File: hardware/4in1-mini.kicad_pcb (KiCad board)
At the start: 6 copper layers, 31.2 x 33 mm, 186 parts, among them J1 SM08B-SRSS-TB, Q1 DOY180N03T, Q10 DOY180N03T, Q11 DOY180N03T, Q12 DOY180N03T, Q13 DOY180N03T, Q14 DOY180N03T, Q15 DOY180N03T, Q16 DOY180N03T, Q17 DOY180N03T, Q18 DOY180N03T, Q19 DOY180N03T, Q2 DOY180N03T, Q20 DOY180N03T, Q21 DOY180N03T, Q22 DOY180N03T, Q23 DOY180N03T, Q24 DOY180N03T, Q3 DOY180N03T, Q4 DOY180N03T, Q5 DOY180N03T, Q6 DOY180N03T, Q7 DOY180N03T, Q8 DOY180N03T, Q9 DOY180N03T, U1 TLV76733DRVR, U10 AT32F421G8U7, U11 NSG2065Q, U12 INA186A3IDCKR, U13 LMR54406DBVR, U2 AT32F421G8U7, U3 NSG2065Q, U5 FTC160808S4R7MBCA, U6 AT32F421G8U7, U7 NSG2065Q, U8 AT32F421G8U7, U9 NSG2065Q

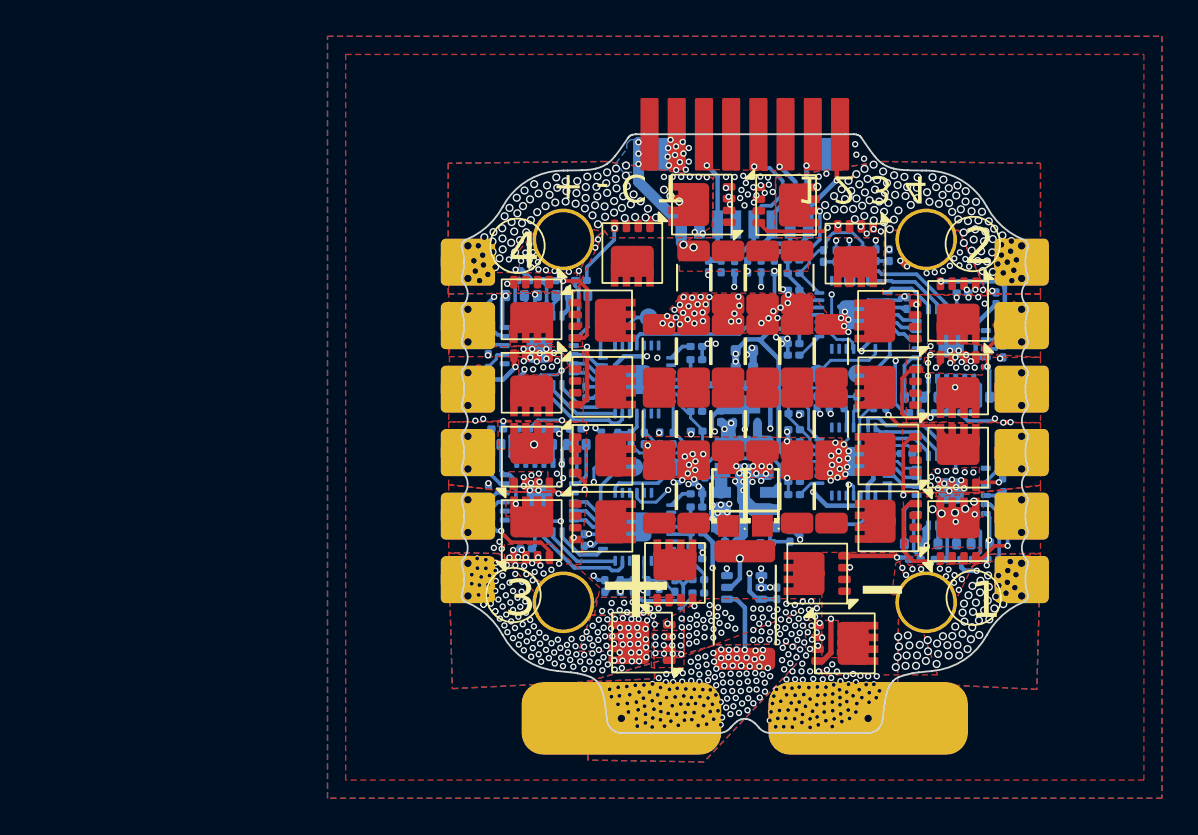
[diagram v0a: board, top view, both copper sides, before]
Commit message: Rev 3: input TVS removed
The 2x SMF24A-T13 are removed. Their 24 V standoff sits below the 25.2 V a full
6S pack reaches, so they conducted rather than protected. The board stays 6S
only and now has no input clamp; DESIGN.md updated to say so.

ERC and DRC reviewed by the maintainer.

Co-Authored-By: Claude Opus 5 (1M context) <noreply@anthropic.com>
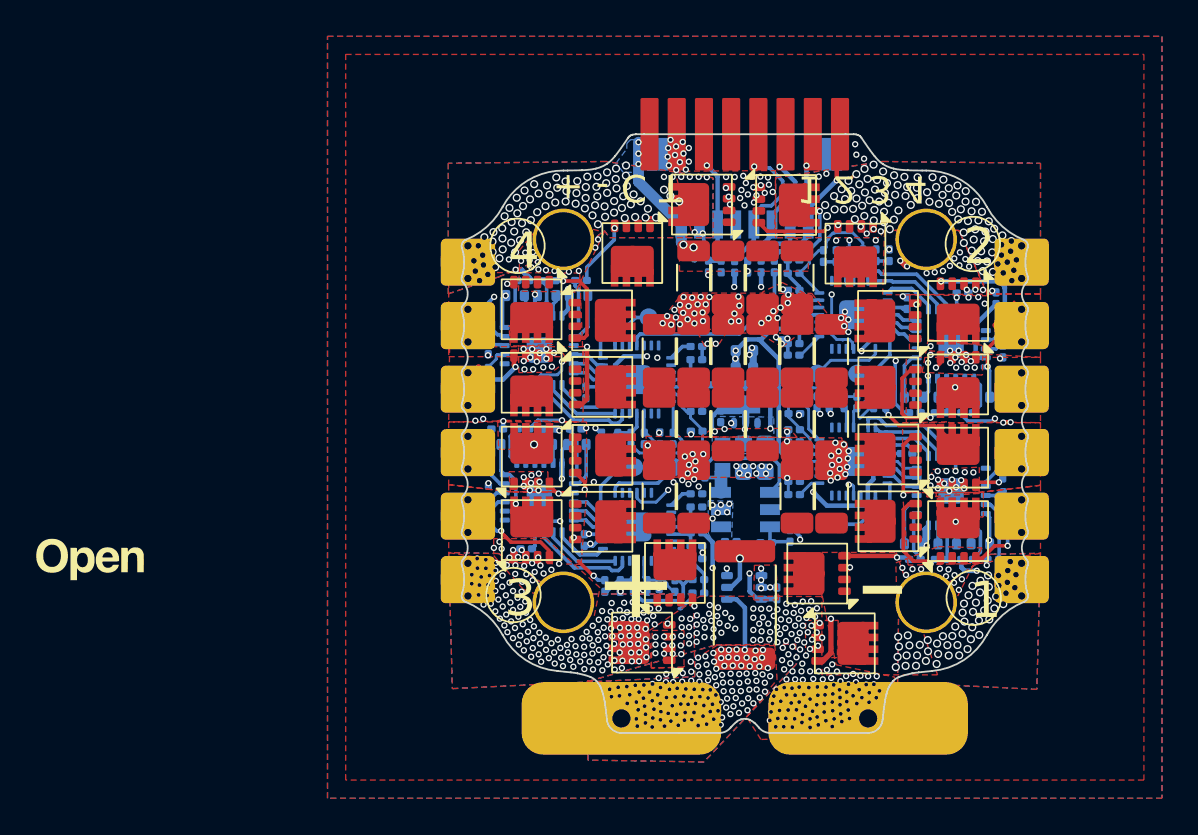
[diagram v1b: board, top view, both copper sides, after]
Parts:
- removed D1, D2: SMF24A-T13, 4in1ESC:SOD-123FL_L2.7-W1.8-LS3.7-RD
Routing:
- net GND: track 75.7 -> 28.5 mm, vias 457 -> 447
- net +10V: track 85.6 -> 78.6 mm
- net /ESC1/MotorB: track 18.8 -> 13.4 mm, vias 8 -> 2
- net +BATT: track 11.6 -> 9.99 mm
- net /ESC3/MotorC: track 13.8 -> 14.9 mm
- net /ESC4/MotorB: track 15.5 -> 14.8 mm
- net /ESC4/MotorA: track 20.1 -> 19.5 mm
- net Net-(Q20-G): track 17.5 -> 16.9 mm
- net /ESC3/MotorA: track 10.7 -> 10.6 mm, vias 144 -> 142
- net Net-(U10-PB4): vias 1 -> 0
- net /ESC2/MotorA: vias 100 -> 99
- net /CSA+: vias 140 -> 137
- added copper zone on B.Cu, net +10V
- added copper zone on In1.Cu, net /ESC1/MotorA
- added copper zone on In4.Cu, net /ESC1/MotorA
- added copper zone on In1.Cu, net /ESC2/MotorA
- added copper zone on In4.Cu, net /ESC2/MotorA
- added copper zone on In1.Cu, net /ESC3/MotorA
- added copper zone on In4.Cu, net /ESC3/MotorA
- added copper zone on In1.Cu, net /ESC4/MotorA
- added copper zone on In4.Cu, net /ESC4/MotorA
- removed copper zone on In2.Cu, net +3V3
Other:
- board text added: "2-6S"
- board text added: "rev3"
- board text removed: "3-6S"

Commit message: Rev 3.1 working state: flashing fixture, QC updates, board work
New 20x20-ESC-Flashing pogo-pin fixture project, MotorTest project file,
QC fixture and main board PCB updates, shop badge on the new gold.
Internal notes and regenerable fixture STEPs stay local via the
repo-specific .gitignore tail.

Co-Authored-By: Claude Opus 5 (1M context) <noreply@anthropic.com>
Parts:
- added CL50: 10uF, Capacitor_SMD:C_1206_3216Metric, F.Cu at (75.1, 52.4)
- added CL51: 10uF, Capacitor_SMD:C_1206_3216Metric, F.Cu at (77.0, 52.4)
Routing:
- net /ESC4/MotorA: vias 85 -> 82

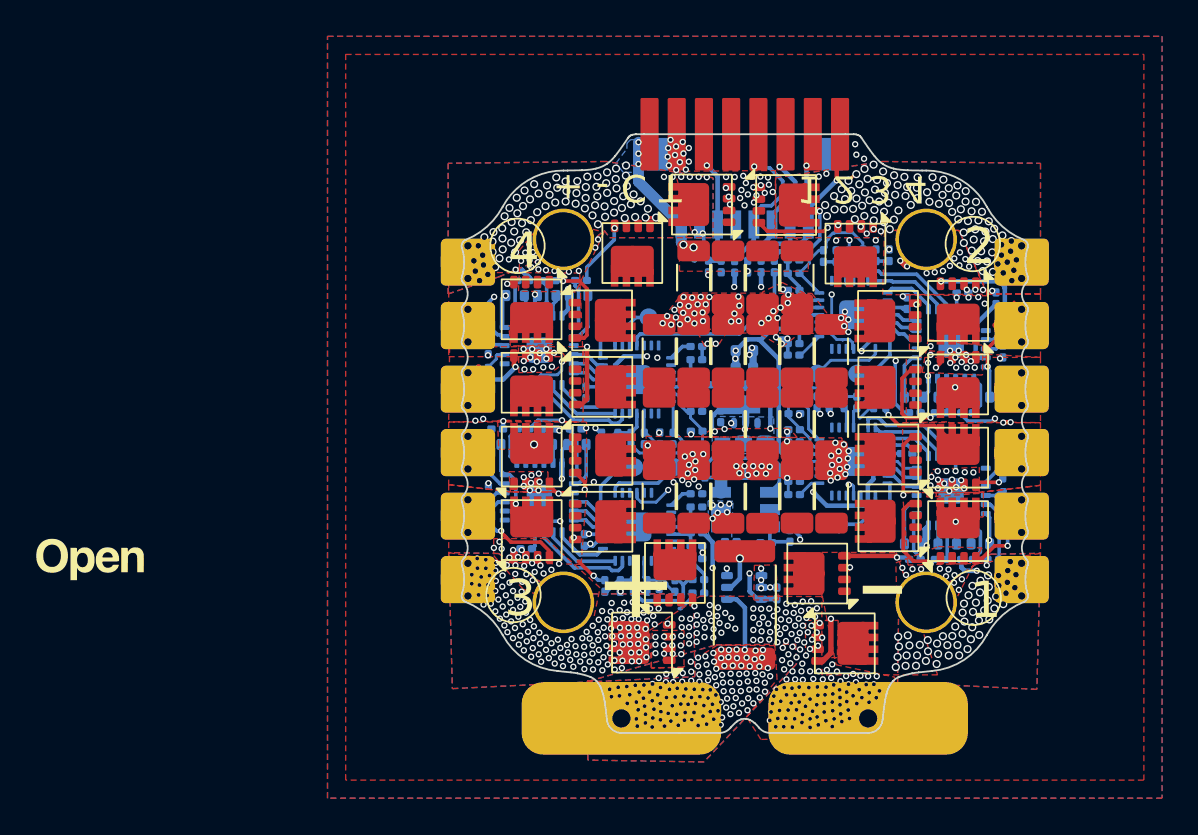
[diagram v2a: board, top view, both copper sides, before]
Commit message: Rev 3.1 release prep: export session state, renders, revisions
The committed board now matches the verified fab export exactly
(check_export.py C1-C3 clean). Renders regenerated from it.

Co-Authored-By: Claude Opus 5 (1M context) <noreply@anthropic.com>
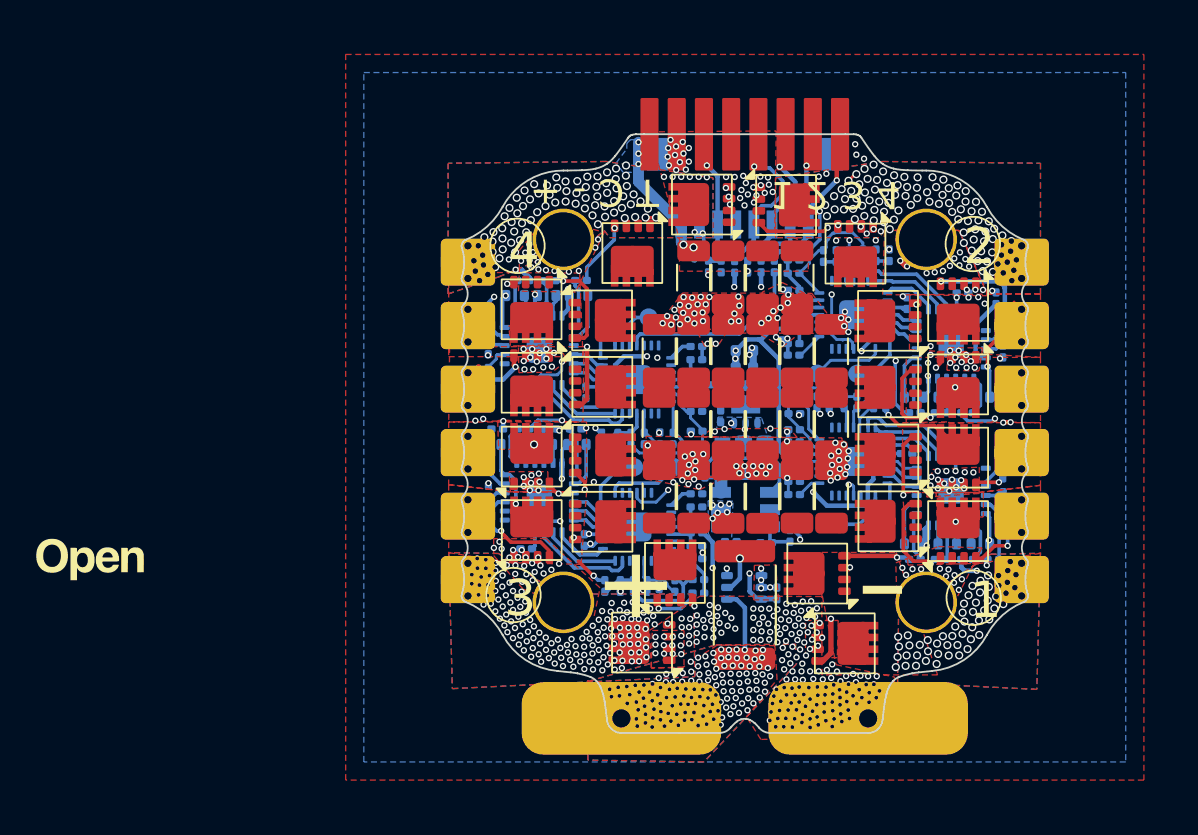
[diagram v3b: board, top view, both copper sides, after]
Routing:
- net GND: track 28.5 -> 19.5 mm
- net /ESC2/MotorC: track 19.1 -> 17.7 mm
- net /ESC3/MotorA: track 10.6 -> 11.7 mm
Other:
- board text added: "T C - +"
- board text added: "rev3.1"
- board text removed: "rev3"

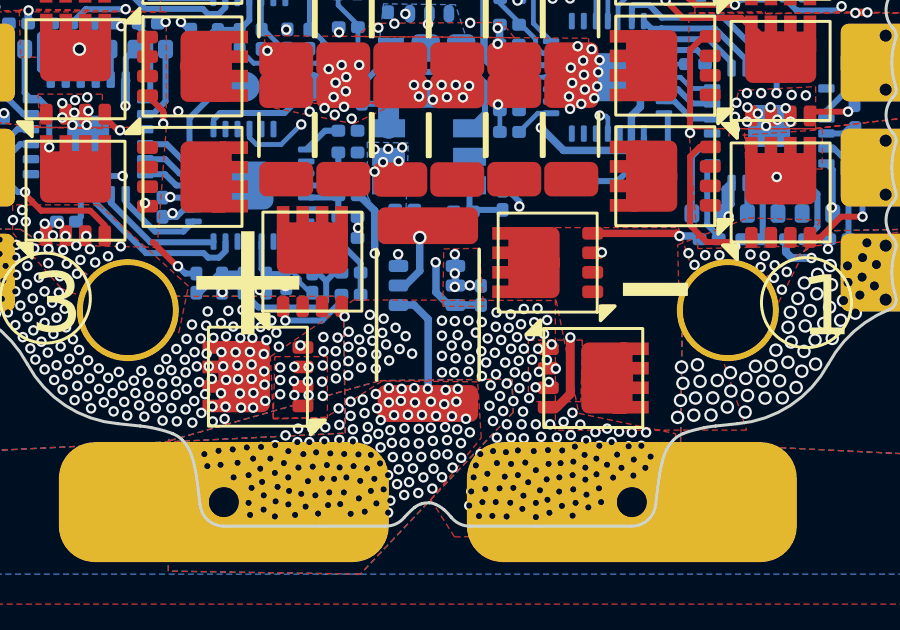
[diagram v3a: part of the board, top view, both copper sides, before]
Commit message: rev3.2: CSA input network against the measured high-side feedthrough
Same change as OpenESC-30x30 rev3.2: R91/R92 1k in the sense legs,
C52/C54 100n 50V to ground, C51 1u across the INA186 inputs. Worst-case
SPICE (1% R, 10% C opposed, 10 Vpp CM at 50 kHz): common-mode at the
pins down 300x, converted differential 2.8 mVpp, DC gain error -0.08
percent. Scale unchanged at 20 mV/A. Acceptance test: the ESC-04
mid-throttle i_a vs clamp sweep that convicted rev3.1
(Logs/esc-04-20x20-20260821T150430Z).

Gates G1-G6 pass with the rev3.2 baselines; fab set 20x20_ESC_Rev3.2
checked consistent against board and schematic. Silkscreen still reads
rev3.1: maintainer edit pending, fab set and renders to be regenerated
after it.

Co-Authored-By: Claude Fable 5 <noreply@anthropic.com>
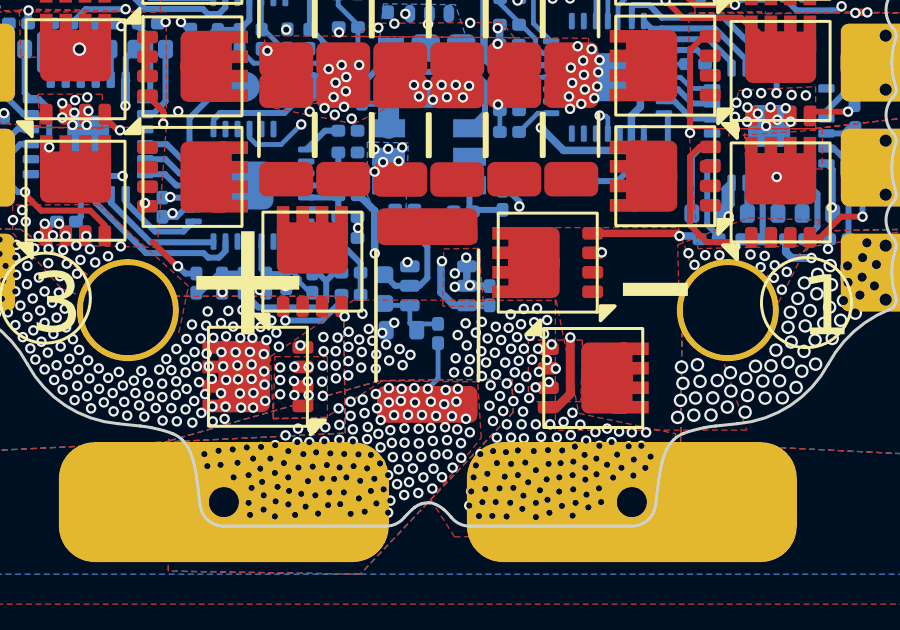
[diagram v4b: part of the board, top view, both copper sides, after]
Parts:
- removed Rsense1: 0.2mR, Resistor_SMD:R_2512_6332Metric
- added C51: 1uF, 4in1ESC-30x30:C_0402_1005Metric, B.Cu at (74.5, 57.5)
- added C52: 100nF, Capacitor_SMD:C_0402_WIDE, B.Cu at (75.1, 58.9)
- added C54: 100nF, Capacitor_SMD:C_0402_WIDE, B.Cu at (76.9, 55.7)
- added R91: 1k, Capacitor_SMD:C_0201_0603Metric, B.Cu at (76.3, 59.0)
- added R92: 1k, Capacitor_SMD:C_0201_0603Metric, B.Cu at (75.2, 55.7)
- added Rsense2: 0.2mR, Resistor_SMD:R_2512_6332Metric, F.Cu at (76.0, 58.4)
- moved U12 0.38 mm to (76.3, 57.4)
- moved C93 0.29 mm to (78.1, 57.7)
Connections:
- U12 pad 4: /CSA+ -> Net-(U12-+IN)
- U12 pad 5: +BATT -> Net-(U12--IN)
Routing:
- net Net-(U12--IN): track 0.00 -> 4.15 mm
- net Net-(U12-+IN): track 0.00 -> 2.61 mm
- net /CSA+: track 3.49 -> 1.66 mm
- net +BATT: track 9.99 -> 8.80 mm, vias 12 -> 11
- net +3V3: track 85.9 -> 86.9 mm
- net Net-(U12-OUT): track 20.8 -> 19.9 mm
- net GND: track 19.5 -> 19.3 mm, vias 447 -> 439
